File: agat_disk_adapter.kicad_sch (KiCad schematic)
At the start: 14 parts, among them J1 IDC‐20, J2 IDC‐20, J3 IDC‐34, J4 IDC‐10, J5 KK‐4

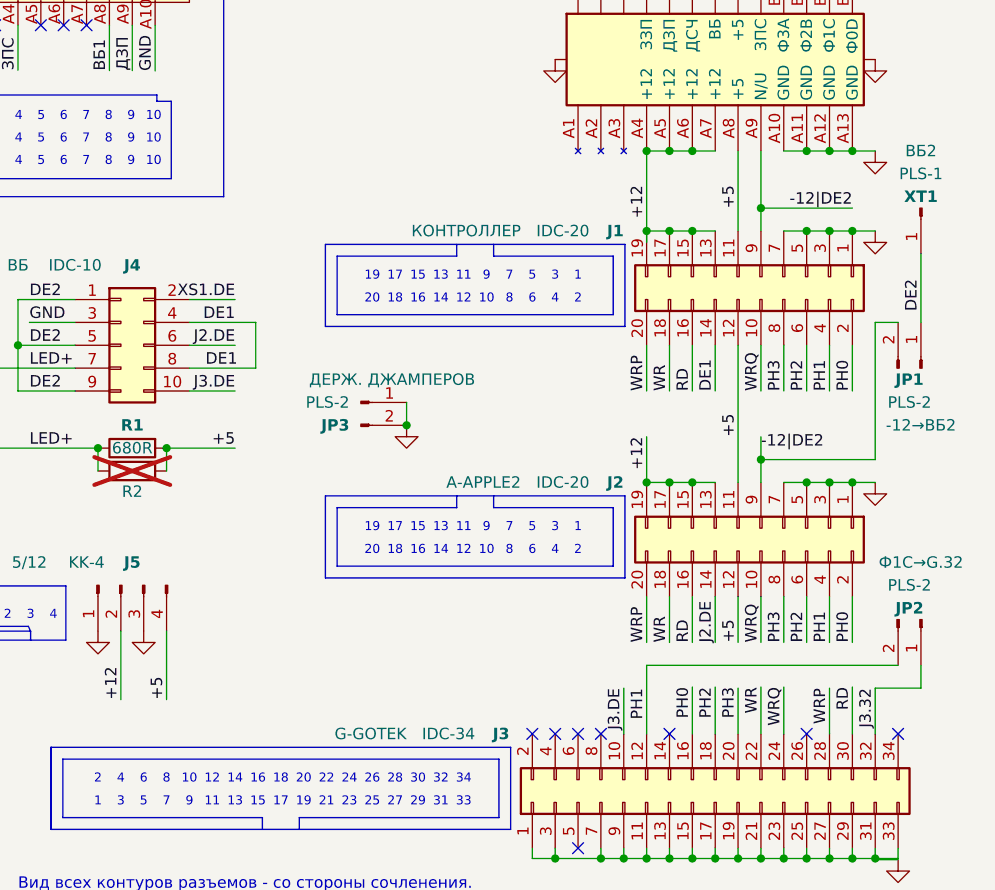
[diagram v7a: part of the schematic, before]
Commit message: slightly improve pcb; fix small drc issues
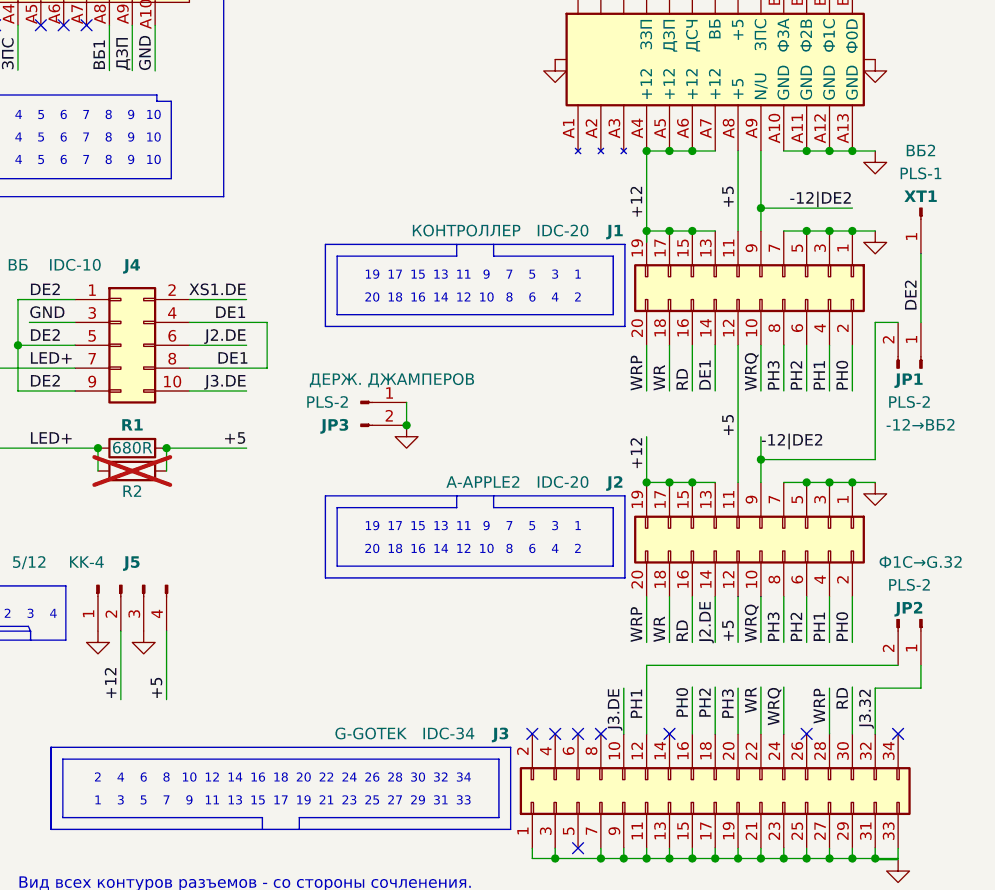
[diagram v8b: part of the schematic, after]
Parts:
- JP1, JP2: value PLS-2 -> PLS‐2
- XP1: footprint (none) -> agat_disk_adapter:Eltra-26M
- XS1: footprint (none) -> agat_disk_adapter:Eltra-26F
- XT1: value PLS-1 -> PLS‐1
- renumbered ~ to XS404
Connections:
- net PH3: now also J3.20 (Pin_20)
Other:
- company: КИБЕР-МУЗЕЙ, МУРОМ -> Михаил Шевченко mike.shevchenko@gmail.com КИБЕР-МУЗЕЙ, МУРОМ
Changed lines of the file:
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@@
 		(date "2026-09")
 		(rev "V1")
-		(company "КИБЕР-МУЗЕЙ, МУРОМ")
+		(company "Михаил Шевченко mike.shevchenko@gmail.com КИБЕР-МУЗЕЙ, МУРОМ")
 		(comment 1 "- Подключение КНГМД - штатным кабелем, либо шлейфом с СНП34-30 на IDC-20,")
 		(comment 2 "- Сигнал \"Выбор Блока\" для 2-го дисковода (ВБ2) можно завести через -12|DE2.")
@@
 	(wire
 		(pts
-			(xy 48.26 96.52) (xy 53.34 96.52)
-		)
-		(stroke
-			(width 0)
-			(type default)
-		)
-	)
-	(wire
-		(pts
 			(xy 111.76 129.54) (xy 111.76 134.62)
 		)
@@
 	(wire
 		(pts
-			(xy 48.26 104.14) (xy 55.626 104.14)
-		)
-		(stroke
-			(width 0)
-			(type default)
-		)
-	)
-	(wire
-		(pts
 			(xy 109.22 101.6) (xy 109.22 116.84)
 		)
@@
 	(wire
 		(pts
-			(xy 44.45 71.1179) (xy 44.45 66.04)
+			(xy 48.26 96.52) (xy 54.61 96.52)
 		)
 		(stroke
@@
 	(wire
 		(pts
-			(xy 121.92 116.84) (xy 124.46 116.84)
+			(xy 44.45 71.1179) (xy 44.45 66.04)
 		)
 		(stroke
@@
 	(wire
 		(pts
-			(xy 104.14 139.573) (xy 104.14 144.78)
+			(xy 121.92 116.84) (xy 124.46 116.84)
 		)
 		(stroke
@@
 	(wire
 		(pts
-			(xy 101.6 88.9) (xy 104.14 88.9)
+			(xy 104.14 139.573) (xy 104.14 144.78)
 		)
 		(stroke
@@
 	(wire
 		(pts
-			(xy 104.14 54.61) (xy 104.14 59.69)
+			(xy 101.6 88.9) (xy 104.14 88.9)
 		)
 		(stroke
@@
 	(wire
 		(pts
-			(xy 99.06 129.54) (xy 99.06 134.62)
+			(xy 104.14 54.61) (xy 104.14 59.69)
 		)
 		(stroke
@@
 	(wire
 		(pts
-			(xy 53.34 113.03) (xy 45.72 113.03)
+			(xy 99.06 129.54) (xy 99.06 134.62)
 		)
 		(stroke
@@
 	(wire
 		(pts
-			(xy 55.626 99.06) (xy 55.626 104.14)
+			(xy 54.61 113.03) (xy 45.72 113.03)
 		)
 		(stroke
@@
 	(wire
 		(pts
-			(xy 124.46 88.9) (xy 121.92 88.9)
+			(xy 56.896 99.06) (xy 56.896 104.14)
 		)
 		(stroke
@@
 	(wire
 		(pts
-			(xy 104.14 158.623) (xy 101.6 158.623)
+			(xy 124.46 88.9) (xy 121.92 88.9)
 		)
 		(stroke
@@
 	(wire
 		(pts
-			(xy 48.26 106.68) (xy 53.34 106.68)
+			(xy 104.14 158.623) (xy 101.6 158.623)
 		)
 		(stroke
@@
 		)
 	)
-	(wire
-		(pts
-			(xy 48.26 99.06) (xy 55.626 99.06)
-		)
-		(stroke
-			(width 0)
-			(type default)
-		)
-	)
 	(polyline
 		(pts
@@
 		)
 	)
+	(wire
+		(pts
+			(xy 48.26 104.14) (xy 56.896 104.14)
+		)
+		(stroke
+			(width 0)
+			(type default)
+		)
+	)
 	(polyline
 		(pts
@@
 	(wire
 		(pts
-			(xy 48.26 101.6) (xy 53.34 101.6)
-		)
-		(stroke
-			(width 0)
-			(type default)
-		)
-	)
-	(wire
-		(pts
 			(xy 119.38 129.54) (xy 119.38 134.62)
 		)
@@
 	(wire
 		(pts
+			(xy 48.26 101.6) (xy 54.61 101.6)
+		)
+		(stroke
+			(width 0)
+			(type default)
+		)
+	)
+	(wire
+		(pts
 			(xy 111.76 101.6) (xy 111.76 106.68)
 		)
@@
 		)
 	)
+	(wire
+		(pts
+			(xy 48.26 99.06) (xy 56.896 99.06)
+		)
+		(stroke
+			(width 0)
+			(type default)
+		)
+	)
 	(polyline
 		(pts
@@
 		)
 	)
+	(wire
+		(pts
+			(xy 48.26 106.68) (xy 54.61 106.68)
+		)
+		(stroke
+			(width 0)
+			(type default)
+		)
+	)
 	(polyline
 		(pts
@@
 	)
 	(label "DE1"
-		(at 53.34 99.06 180)
+		(at 54.61 99.06 180)
 		(effects
 			(font
@@
 	)
 	(label "XS1.DE"
-		(at 53.34 96.52 180)
+		(at 54.61 96.52 180)
 		(effects
 			(font
@@
 	)
 	(label "+5"
-		(at 53.34 113.03 180)
+		(at 54.61 113.03 180)
 		(effects
 			(font
@@
 	)
 	(label "J3.DE"
-		(at 53.34 106.68 180)
+		(at 54.61 106.68 180)
 		(effects
 			(font
@@
 	)
 	(label "J2.DE"
-		(at 53.34 101.6 180)
+		(at 54.61 101.6 180)
 		(effects
 			(font
@@
 	)
 	(label "PH3"
-		(at 109.22 139.573 270)
+		(at 109.22 139.7 270)
 		(effects
 			(font
@@
 	)
 	(label "DE1"
-		(at 53.594 104.14 180)
+		(at 54.864 104.14 180)
 		(effects
 			(font
@@
 			)
 		)
-		(property "Footprint" ""
+		(property "Footprint" "agat_disk_adapter:Eltra-26M"
 			(at 91.44 74.93 0)
 			(hide yes)
@@
 		(in_pos_files no)
 		(dnp no)
-		(property "Reference" "~"
+		(property "Reference" "XS404"
 			(at 15.875 60.325 0)
 			(hide yes)
@@
 			(project "agat_disk_adapter"
 				(path "/e6908ff4-84b7-4cdb-b4c1-fd2e829eca09"
-					(reference "~")
+					(reference "XS404")
 					(unit 1)
 				)
@@
 			)
 		)
-		(property "Footprint" ""
+		(property "Footprint" "agat_disk_adapter:Eltra-26F"
 			(at 91.44 39.37 0)
 			(hide yes)
@@
 			)
 		)
-		(property "Value" "PLS-2"
+		(property "Value" "PLS‐2"
 			(at 128.27 128.27 90)
 			(show_name no)
@@
 			)
 		)
-		(property "Value" "PLS-1"
+		(property "Value" "PLS‐1"
 			(at 129.54 82.55 90)
 			(show_name no)
@@
 		(in_pos_files no)
 		(dnp no)
-		(property "Reference" "~"
+		(property "Reference" "XS404"
 			(at 15.875 45.085 0)
 			(hide yes)
@@
 			(project "agat_disk_adapter"
 				(path "/e6908ff4-84b7-4cdb-b4c1-fd2e829eca09"
-					(reference "~")
+					(reference "XS404")
 					(unit 2)
 				)
@@
 		(in_pos_files no)
 		(dnp no)
-		(property "Reference" "~"
+		(property "Reference" "XS404"
 			(at 15.875 29.845 0)
 			(hide yes)
@@
 			(project "agat_disk_adapter"
 				(path "/e6908ff4-84b7-4cdb-b4c1-fd2e829eca09"
-					(reference "~")
+					(reference "XS404")
 					(unit 3)
 				)
@@
 			)
 		)
-		(property "Value" "PLS-2"
+		(property "Value" "PLS‐2"
 			(at 128.27 107.95 90)
 			(show_name no)
